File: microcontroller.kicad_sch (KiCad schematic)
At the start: 13 parts, among them SW1 Boot Switch, SW2 System Reset, U2 STM32F401RETx

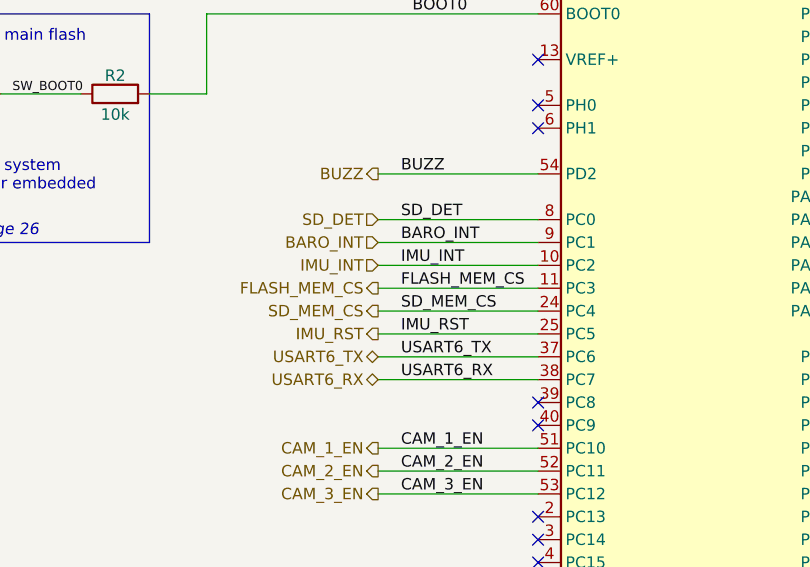
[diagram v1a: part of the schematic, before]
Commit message: Adi made some fixes to schematic
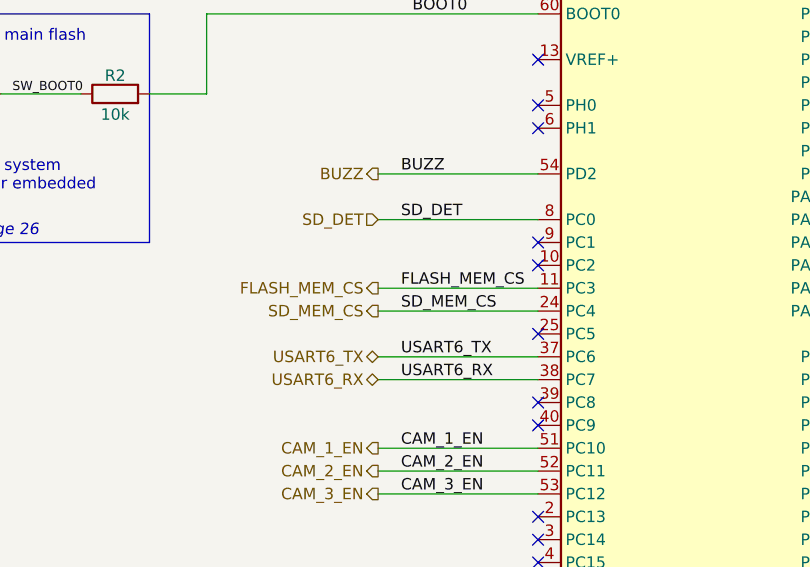
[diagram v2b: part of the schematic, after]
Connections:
- net BARO_INT: no longer names the net of U2.9 (PC1)
- net IMU_INT: no longer names the net of U2.10 (PC2)
- net IMU_RST: no longer names the net of U2.25 (PC5)
- no-connect marks 24 -> 27
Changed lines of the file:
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@@
 	)
 	(no_connect
+		(at 110.49 106.68)
+	)
+	(no_connect
+		(at 110.49 109.22)
+	)
+	(no_connect
 		(at 110.49 137.16)
 	)
@@
 	)
 	(no_connect
+		(at 110.49 116.84)
+	)
+	(no_connect
 		(at 146.05 144.78)
 	)
@@
 		)
 	)
-	(wire
-		(pts
-			(xy 92.71 109.22) (xy 110.49 109.22)
-		)
-		(stroke
-			(width 0)
-			(type default)
-		)
-	)
 	(polyline
 		(pts
@@
 	(wire
 		(pts
-			(xy 92.71 106.68) (xy 110.49 106.68)
-		)
-		(stroke
-			(width 0)
-			(type default)
-		)
-	)
-	(wire
-		(pts
 			(xy 146.05 76.2) (xy 177.8 76.2)
 		)
@@
 	(wire
 		(pts
-			(xy 92.71 116.84) (xy 110.49 116.84)
-		)
-		(stroke
-			(width 0)
-			(type default)
-		)
-	)
-	(wire
-		(pts
 			(xy 128.27 162.56) (xy 128.27 165.1)
 		)
@@
 		)
 	)
-	(label "BARO_INT"
-		(at 95.25 106.68 0)
-		(effects
-			(font
-				(size 1.27 1.27)
-			)
-			(justify left bottom)
-		)
-	)
 	(label "12C1_SDA"
 		(at 154.94 142.24 0)
@@
 		)
 	)
-	(label "IMU_RST"
-		(at 95.25 116.84 0)
-		(effects
-			(font
-				(size 1.27 1.27)
-			)
-			(justify left bottom)
-		)
-	)
 	(label "SYS_JTCK-SWCLK"
 		(at 154.94 111.76 0)
@@
 		)
 	)
-	(label "IMU_INT"
-		(at 95.25 109.22 0)
-		(effects
-			(font
-				(size 1.27 1.27)
-			)
-			(justify left bottom)
-		)
-	)
 	(label "NRST"
 		(at 96.52 76.2 0)
@@
 		)
 	)
-	(hierarchical_label "BARO_INT"
-		(shape input)
-		(at 92.71 106.68 180)
-		(effects
-			(font
-				(size 1.27 1.27)
-			)
-			(justify right)
-		)
-	)
-	(hierarchical_label "IMU_RST"
-		(shape output)
-		(at 92.71 116.84 180)
-		(effects
-			(font
-				(size 1.27 1.27)
-			)
-			(justify right)
-		)
-	)
 	(hierarchical_label "FLASH_MEM_CS"
 		(shape output)
@@
 		(effects
 			(font
-				(size 1.27 1.27)
-			)
-			(justify right)
-		)
-	)
-	(hierarchical_label "IMU_INT"
-		(shape input)
-		(at 92.71 109.22 180)
-		(effects
-			(font

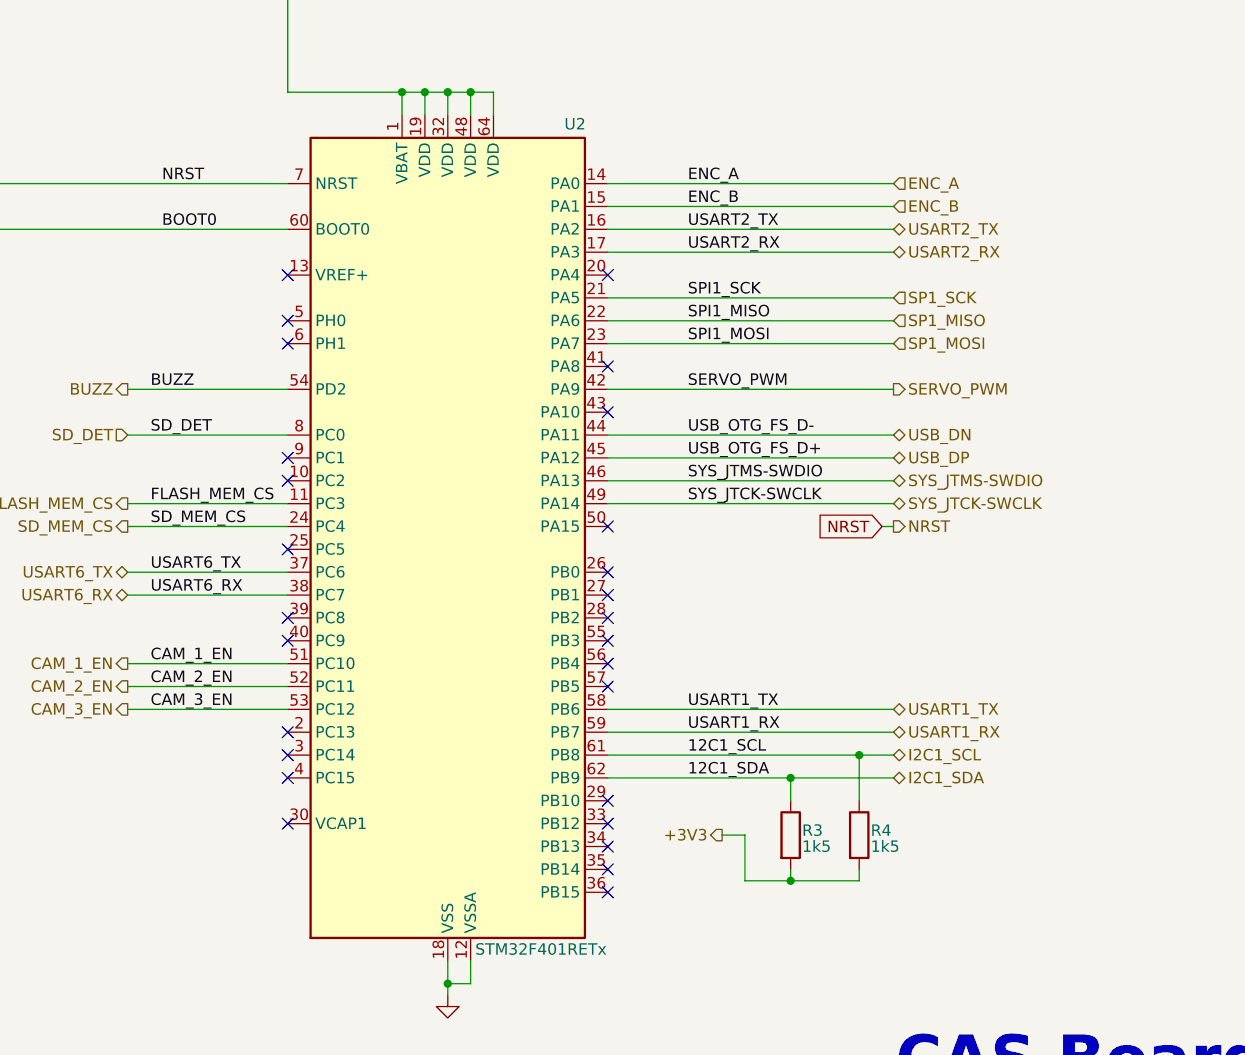
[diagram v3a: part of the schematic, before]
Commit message: Revised to improve buck converters and free up space on board
Fixed overvoltage error on encoder (5v -> 3v)
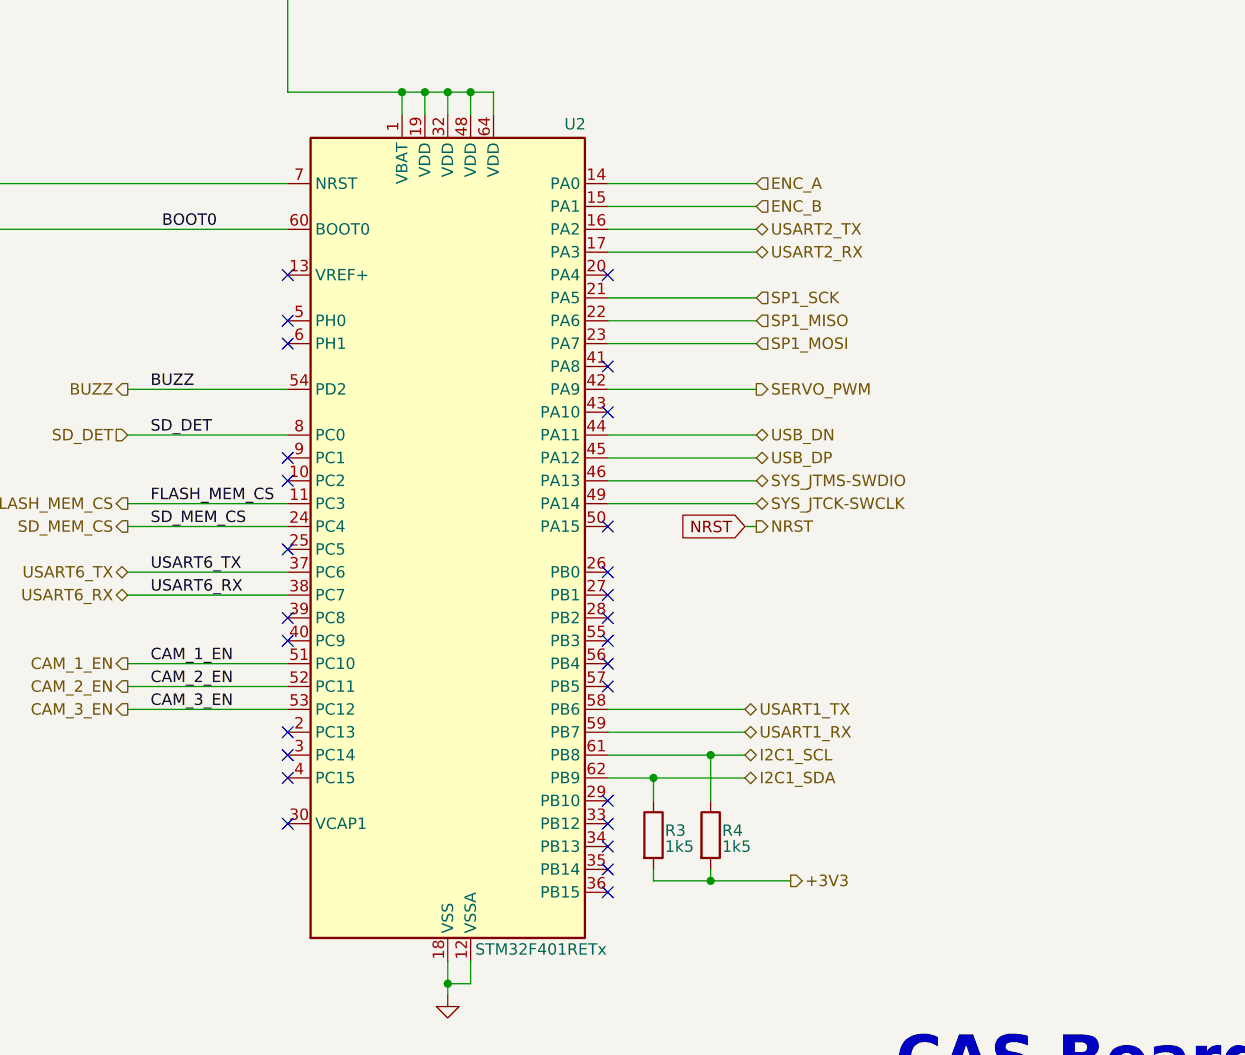
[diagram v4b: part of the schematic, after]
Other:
- moved on the sheet: R3, R4

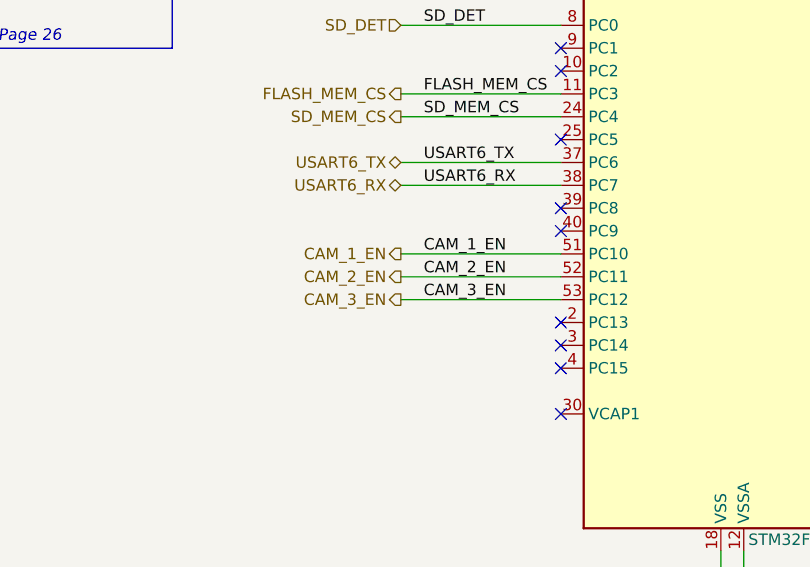
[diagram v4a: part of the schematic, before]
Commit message: Revised routing
Minor changes to signal routing. Cleared out drc errors
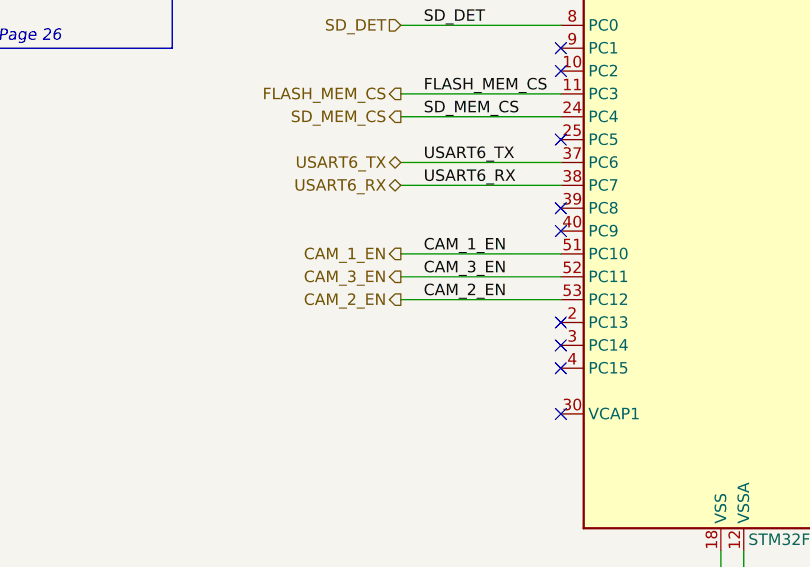
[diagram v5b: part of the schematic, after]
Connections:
- net CAM_2_EN: now also U2.53 (PC12); no longer U2.52 (PC11)
- net CAM_3_EN: now also U2.52 (PC11); no longer U2.53 (PC12)
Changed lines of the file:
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@@
 	(wire
 		(pts
-			(xy 151.13 142.24) (xy 161.29 142.24)
+			(xy 92.71 134.62) (xy 110.49 134.62)
 		)
 		(stroke
@@
 	(wire
 		(pts
-			(xy 130.81 68.58) (xy 130.81 66.04)
+			(xy 151.13 142.24) (xy 161.29 142.24)
 		)
 		(stroke
@@
 	(wire
 		(pts
-			(xy 72.39 36.83) (xy 85.09 36.83)
+			(xy 130.81 68.58) (xy 130.81 66.04)
 		)
 		(stroke
@@
 	(wire
 		(pts
-			(xy 35.56 92.71) (xy 40.64 92.71)
+			(xy 72.39 36.83) (xy 85.09 36.83)
 		)
 		(stroke
@@
 	(wire
 		(pts
-			(xy 146.05 78.74) (xy 162.56 78.74)
+			(xy 35.56 92.71) (xy 40.64 92.71)
 		)
 		(stroke
@@
 	(wire
 		(pts
-			(xy 85.09 26.67) (xy 97.79 26.67)
+			(xy 146.05 78.74) (xy 162.56 78.74)
 		)
 		(stroke
@@
 	(wire
 		(pts
-			(xy 73.66 81.28) (xy 110.49 81.28)
+			(xy 85.09 26.67) (xy 97.79 26.67)
 		)
 		(stroke
@@
 	(wire
 		(pts
-			(xy 92.71 132.08) (xy 110.49 132.08)
+			(xy 73.66 81.28) (xy 110.49 81.28)
 		)
 		(stroke
@@
 	(wire
 		(pts
+			(xy 92.71 132.08) (xy 110.49 132.08)
+		)
+		(stroke
+			(width 0)
+			(type default)
+		)
+	)
+	(wire
+		(pts
 			(xy 92.71 119.38) (xy 110.49 119.38)
 		)
@@
 	(wire
 		(pts
-			(xy 92.71 134.62) (xy 110.49 134.62)
-		)
-		(stroke
-			(width 0)
-			(type default)
-		)
-	)
-	(wire
-		(pts
 			(xy 110.49 26.67) (xy 110.49 66.04)
 		)
@@
 		)
 	)
-	(label "CAM_3_EN"
-		(at 95.25 134.62 0)
-		(effects
-			(font
-				(size 1.27 1.27)
-			)
-			(justify left bottom)
-		)
-	)
 	(label "SD_DET"
 		(at 95.25 104.14 0)
@@
 		)
 	)
-	(label "SD_MEM_CS"
-		(at 95.25 114.3 0)
+	(label "CAM_3_EN"
+		(at 95.25 132.08 0)
 		(effects
 			(font
@@
 		)
 	)
-	(label "CAM_2_EN"
-		(at 95.25 132.08 0)
+	(label "SD_MEM_CS"
+		(at 95.25 114.3 0)
 		(effects
 			(font
@@
 		)
 	)
+	(label "CAM_2_EN"
+		(at 95.25 134.62 0)
+		(effects
+			(font
+				(size 1.27 1.27)
+			)
+			(justify left bottom)
+		)
+	)
 	(label "CAM_1_EN"
 		(at 95.25 129.54 0)
@@
 	(hierarchical_label "CAM_2_EN"
 		(shape output)
-		(at 92.71 132.08 180)
+		(at 92.71 134.62 180)
 		(effects
 			(font
@@
 		)
 	)
-	(hierarchical_label "CAM_3_EN"
-		(shape output)
-		(at 92.71 134.62 180)
-		(effects
-			(font
-				(size 1.27 1.27)
-			)
-			(justify right)
-		)
-	)
 	(hierarchical_label "USART1_TX"
 		(shape bidirectional)
@@
 		(effects
 			(font
+				(size 1.27 1.27)
+			)
+			(justify right)
+		)
+	)
+	(hierarchical_label "CAM_3_EN"
+		(shape output)
+		(at 92.71 132.08 180)
+		(effects
+			(font
